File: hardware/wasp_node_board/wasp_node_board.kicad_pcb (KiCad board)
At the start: 4 copper layers, 115 parts, among them J1 Conn_01x02, J2 RJ45_Hanrun_HR911105A_Horizon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, J3 Conn_02x10_Odd_Even, J4 RJ45_Hanrun_HR911105A_Horizon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, J5 RJ45_Hanrun_HR911105A_Horizon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, J6 TC2030, J7 USB_C_Receptacle_USB2.0_16P, SW1 C&K JS102011SAQN, SW2 C&K KMR231NG LFS, U1 STM32H723ZGTx, U2 USBLC6-2SC6, U3 APS6404L-3SQRx-SN, U4 TPSM863253RDXR, U5 KSZ8794CNXCC, U6 LP5907MFX-1.2, Y1 TSX-3225 25.00M-N0YYYYG30RGB, Y2 ASE-25.000MHZ-L-K-T

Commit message: Layout half way done, starting an experiment
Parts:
- R25, Y2: moved to B.Cu
- moved J3 90.9 mm to (103.9, 54.3), turned to 0 degrees
- moved C7 86.3 mm to (126.7, 102.7), turned to 90 degrees
- moved C4 86.1 mm to (125.7, 99.0)
- moved R4 86.1 mm to (126.7, 99.0)
- moved C20 86.1 mm to (122.1, 97.7)
- moved C24 86.1 mm to (122.1, 103.2)
- moved Y1 86.1 mm to (122.1, 100.5)
- moved FB5 85.8 mm to (122.2, 93.3)
- moved C3 85.6 mm to (130.3, 102.9)
- moved C12 85.2 mm to (144.5, 55.9)
- moved C13 85.2 mm to (142.5, 55.9)
- moved C22 85.2 mm to (131.6, 53.5)
- moved C25 85.2 mm to (140.5, 55.9)
- moved C39 85.2 mm to (151.1, 55.8)
- moved C40 85.2 mm to (153.1, 55.8)
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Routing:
- net GND: track 0.00 -> 75.2 mm, vias 0 -> 34
- net Net-(U5-LED1_0): track 0.00 -> 49.0 mm, vias 0 -> 2
- net VDD12D: track 0.00 -> 41.6 mm, vias 0 -> 4
- net VDDAT: track 0.00 -> 40.8 mm, vias 0 -> 5
- net Net-(U5-LED3_1): track 0.00 -> 39.1 mm
- net /mcu/PG12: track 0.00 -> 37.2 mm, vias 0 -> 1
- net VDDIO: track 0.00 -> 36.3 mm, vias 0 -> 3
- net Net-(U5-LED2_1): track 0.00 -> 34.8 mm, vias 0 -> 2
- net /ethernet/RX1_P: track 0.00 -> 33.2 mm
- net /ethernet/RX1_N: track 0.00 -> 33.1 mm
- net ETH_RXD1: track 0.00 -> 32.1 mm, vias 0 -> 2
- net ETH_RXD0: track 0.00 -> 31.8 mm, vias 0 -> 2
- net Net-(U5-LED1_1): track 0.00 -> 31.2 mm, vias 0 -> 2
- net ETH_CRS_DV: track 0.00 -> 31.2 mm, vias 0 -> 2
- net USB_D_P: track 6.56 -> 36.6 mm
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- added copper zone on In2.Cu, net +3V3
- added copper zone on In1.Cu, net GND
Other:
- board outline added: 63.5 x 82.5 mm

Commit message: Removed some stuff and got the general placement down
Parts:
- removed A1: Arduino_UNO_R3, Arduino_UNO_R3_Headers:Arduino_UNO_R3_Headers
- removed J3: Conn_02x10_Odd_Even, Connector_PinHeader_2.54mm:PinHeader_2x10_P2.54mm_Vertical
- C22, C35, C36, C37, C38, C41, C42, C43, C44, C45, C46, C47, C48, C49, C50, C51, C52, C53, C54, C55, C56, C57, C58, C59, C60, FL1, J6, J7, R1, R2, R24, R5, U1, U2, U3: moved to B.Cu
- moved J7 60.3 mm to (158.4, 98.8), turned to -90 degrees
- moved J6 56.7 mm to (148.1, 104.1), turned to 0 degrees
- moved R2 55.4 mm to (152.6, 101.0), turned to -90 degrees
- moved C35 51.1 mm to (106.6, 85.2)
- moved U2 50.0 mm to (150.6, 99.0), turned to -90 degrees
- moved R1 49.9 mm to (152.6, 97.0), turned to 90 degrees
- moved C36 48.6 mm to (107.9, 84.6)
- moved C22 45.7 mm to (152.1, 94.3), turned to -90 degrees
- moved FL1 45.4 mm to (147.1, 99.1), turned to 180 degrees
- moved U3 43.4 mm to (110.7, 90.5), turned to 180 degrees
- moved C37 40.0 mm to (115.1, 83.7), turned to 180 degrees
- moved C43 38.5 mm to (113.3, 105.0), turned to 180 degrees
- moved Y2 38.1 mm to (110.5, 98.8)
- moved R25 38.1 mm to (112.8, 98.2)
- moved C44 38.0 mm to (113.6, 107.0), turned to 180 degrees
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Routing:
- net GND: track 75.2 -> 0.07 mm, vias 34 -> 0
- net Net-(U5-LED1_0): track 49.0 -> 0.00 mm, vias 2 -> 0
- net VDD12D: track 41.6 -> 0.00 mm, vias 4 -> 0
- net VDDAT: track 40.8 -> 0.00 mm, vias 5 -> 0
- net Net-(U5-LED3_1): track 39.1 -> 0.00 mm
- net /mcu/PG12: track 37.2 -> 0.00 mm, vias 1 -> 0
- net USB_D_P: track 36.6 -> 0.00 mm
- net USB_D_N: track 36.6 -> 0.00 mm
- net VDDIO: track 36.3 -> 0.00 mm, vias 3 -> 0
- net Net-(U5-LED2_1): track 34.8 -> 0.00 mm, vias 2 -> 0
- net ETH_RXD1: track 32.1 -> 0.00 mm, vias 2 -> 0
- net ETH_RXD0: track 31.8 -> 0.00 mm, vias 2 -> 0
- net Net-(U5-LED1_1): track 31.2 -> 0.00 mm, vias 2 -> 0
- net ETH_CRS_DV: track 31.2 -> 0.00 mm, vias 2 -> 0
- net +3V3: track 29.5 -> 0.00 mm, vias 12 -> 0
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- removed copper zone on In2.Cu, net +3V3
- removed copper zone on In1.Cu, net GND
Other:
- board size 63.5 x 82.5 mm -> 59.2 x 51.4 mm

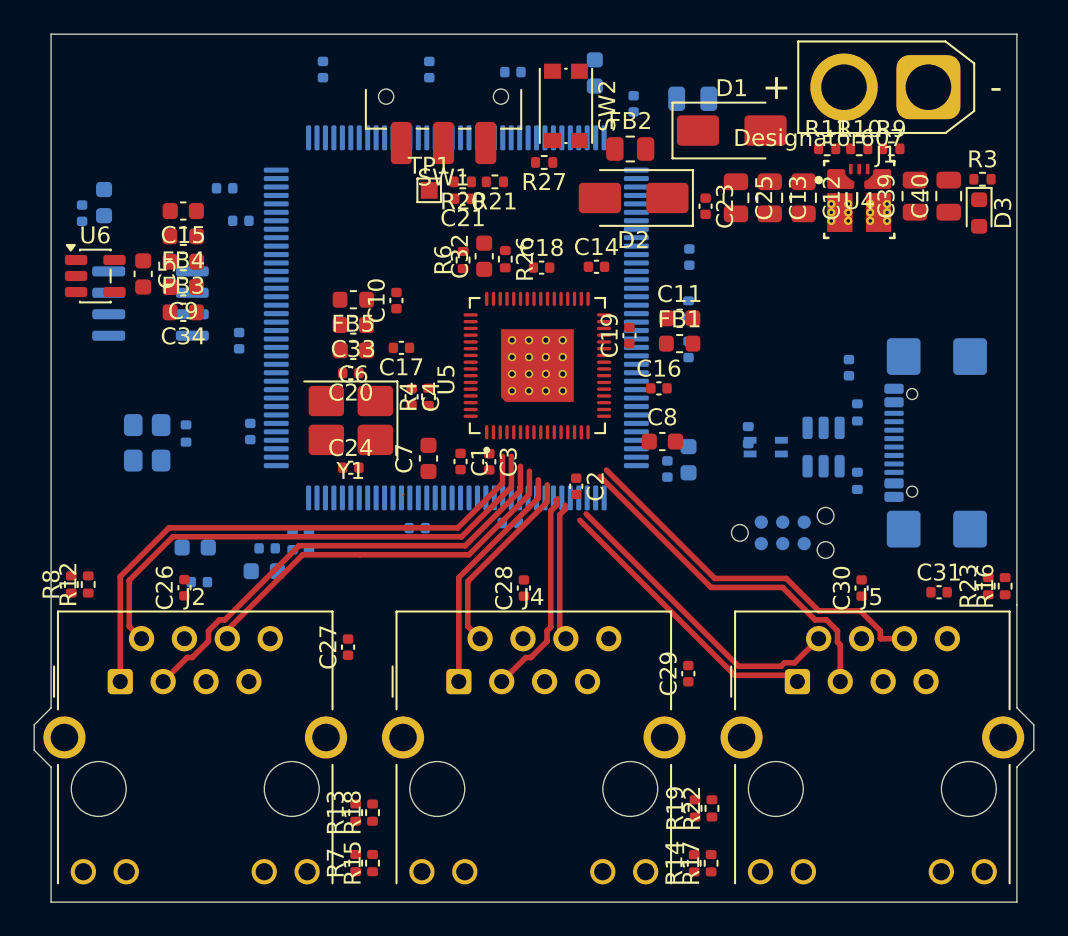
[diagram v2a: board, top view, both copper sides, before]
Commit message: Layout candidate done. Now to add back some functionality
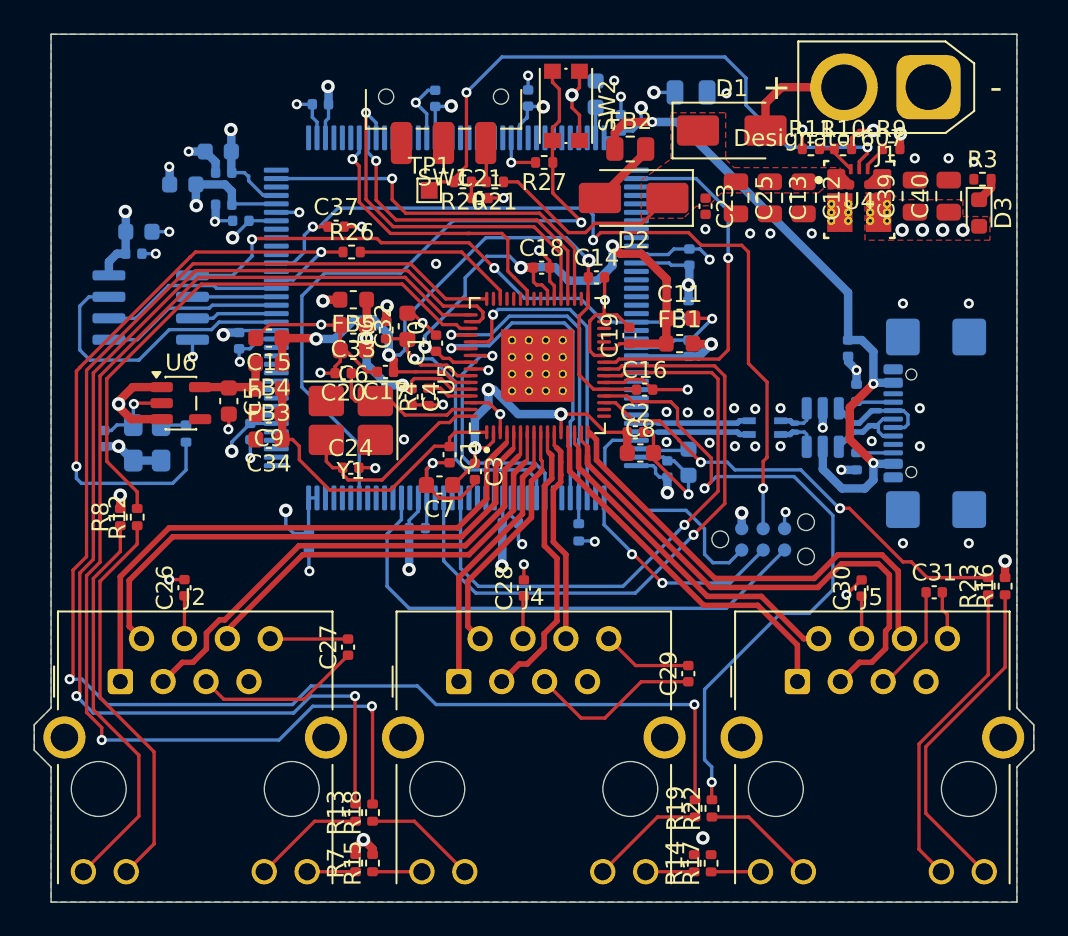
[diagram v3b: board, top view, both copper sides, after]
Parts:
- C37: moved to F.Cu
- moved C41 32.5 mm to (108.0, 98.5), turned to 90 degrees
- moved C47 29.7 mm to (133.1, 78.4), turned to 90 degrees
- moved C43 23.5 mm to (114.7, 81.5)
- moved C45 23.4 mm to (112.6, 83.5)
- moved C46 22.4 mm to (115.0, 82.8)
- moved C44 22.4 mm to (115.0, 84.7)
- moved R5 11.6 mm to (136.1, 104.1)
- moved R26 9.11 mm to (122.6, 87.5), turned to 0 degrees
- moved C15 9.08 mm to (117.7, 92.6)
- moved C34 9.08 mm to (117.7, 98.6)
- moved C5 9.08 mm to (115.3, 96.3)
- moved C9 9.08 mm to (117.7, 97.1)
- moved FB3 9.08 mm to (117.7, 95.6)
- moved FB4 9.08 mm to (117.7, 94.1)
- moved U6 9.08 mm to (112.5, 96.5)
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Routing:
- net GND: track 0.07 -> 129.6 mm, vias 0 -> 72
- net +3V3: track 0.00 -> 93.5 mm, vias 0 -> 33
- net Net-(U5-LED2_1): track 0.00 -> 90.1 mm, vias 0 -> 2
- net Net-(U5-LED1_1): track 0.00 -> 71.0 mm, vias 0 -> 2
- net Net-(U5-LED2_0): track 0.00 -> 70.4 mm, vias 0 -> 2
- net /mcu/JTAG_NRST: track 0.00 -> 50.1 mm, vias 0 -> 3
- net VDD12D: track 0.00 -> 43.0 mm, vias 0 -> 3
- net /mcu/BOOT0: track 0.00 -> 41.8 mm, vias 0 -> 1
- net Net-(U5-LED3_0): track 0.00 -> 40.4 mm, vias 0 -> 2
- net /power/USB_POWER_IN: track 0.00 -> 40.0 mm, vias 0 -> 3
- net ETH_TXD0: track 0.00 -> 38.4 mm, vias 0 -> 1
- net /mcu/PH0/REFCLK: track 0.00 -> 37.0 mm, vias 0 -> 2
- net /power/PWR_EN: track 0.00 -> 36.6 mm, vias 0 -> 2
- net ETH_TXEN: track 0.00 -> 35.8 mm, vias 0 -> 1
- net VDDIO: track 0.00 -> 34.3 mm, vias 0 -> 3
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- added copper zone on F.Cu, net +3V3
- added copper zone on In2.Cu, net +3V3
- added copper zone on F.Cu, net +5V
- added copper zone on B.Cu, net GND
- added copper zone on F.Cu, net GND
- added copper zone on In1.Cu, net GND
- added copper zone on In2.Cu, net GND

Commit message: V1 layout done
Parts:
- removed TP1: TestPoint, TestPoint:TestPoint_Pad_1.0x1.0mm
- added D4: LTST-C191KSKT, LED_SMD:LED_0603_1608Metric, F.Cu at (121.0, 77.5)
- added J8: Conn_02x05_Odd_Even, Connector_PinHeader_2.54mm:PinHeader_2x05_P2.54mm_Vertical_SMD, F.Cu at (112.5, 83.0)
- added J9: Conn_02x05_Odd_Even, Connector_PinHeader_2.54mm:PinHeader_2x05_P2.54mm_Vertical_SMD, F.Cu at (153.1, 93.7)
- added R28: 1k, Resistor_SMD:R_0402_1005Metric, F.Cu at (121.0, 81.0)
- C21, R20, R21: moved to B.Cu
- moved R20 19.5 mm to (147.9, 77.8), turned to 0 degrees
- moved C21 17.6 mm to (146.9, 78.8), turned to 180 degrees
- moved R21 15.9 mm to (146.0, 77.8), turned to 0 degrees
- moved C53 1.15 mm to (141.4, 87.8)
- moved R16 0.70 mm to (160.6, 107.3)
- moved R23 0.70 mm to (159.6, 107.3)
- moved C43 0.30 mm to (114.7, 81.2)
- moved C46 0.30 mm to (115.0, 82.5)
- moved R13 0.25 mm to (122.8, 120.5)
- moved R18 0.25 mm to (123.8, 120.5)
- moved C37 0.15 mm to (121.5, 86.0)
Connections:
- U1 pad 136: /mcu/PB6 -> /mcu/LPUART1_TX
- U1 pad 137: /mcu/PB7 -> /mcu/LPUART1_RX
- U1 pad 46: unconnected-(U1-PB0-Pad46) -> /mcu/status_led
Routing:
- net /mcu/LPUART1_RX: track 0.00 -> 48.1 mm, vias 0 -> 1
- net /mcu/LPUART1_TX: track 0.00 -> 42.2 mm, vias 0 -> 1
- net /mcu/I2C2_SDA: track 0.00 -> 37.7 mm, vias 0 -> 1
- net /mcu/PB5: track 0.00 -> 33.0 mm, vias 0 -> 1
- net /mcu/SPI2_MISO: track 0.00 -> 28.0 mm, vias 0 -> 1
- net /power/PWR_EN: track 36.6 -> 9.33 mm, vias 2 -> 1
- net /mcu/SPI2_CS: track 0.00 -> 26.0 mm, vias 0 -> 1
- net /mcu/I2C2_SCL: track 0.00 -> 25.3 mm, vias 0 -> 1
- net /mcu/SPI2_SCK: track 0.00 -> 24.0 mm, vias 0 -> 1
- net /mcu/USART3_RX: track 0.00 -> 21.7 mm, vias 0 -> 1
- net /mcu/PE9: track 0.00 -> 21.5 mm, vias 0 -> 1
- net /mcu/SPI2_MOSI: track 0.00 -> 20.8 mm, vias 0 -> 1
- net Net-(SW1-A): track 4.20 -> 23.5 mm, vias 0 -> 1
- net /mcu/USART3_TX: track 0.00 -> 15.8 mm, vias 0 -> 1
- net /mcu/PA8: track 0.00 -> 14.2 mm, vias 0 -> 1
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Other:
- board size 59.2 x 51.4 mm -> 60.4 x 51.4 mm
- board text added: "3V3"
- board text added: "BOOTSEL"
- board text added: "CSn2"
- board text added: "ETH 1"
- board text added: "ETH 2"
- board text added: "ETH 3"
- board text added: "GND"
- board text added: "MISO2"
- board text added: "MOSI2"
- board text added: "ON|OFF"
- board text added: "PA0"
- board text added: "PA8"
- board text added: "PB5"
- board text added: "PE9"
- board text added: "SCL2"
- board text added: "SCLK2"
- board text added: "SDA2"
- board text added: "STATUS"
- board text added: "U1RX"
- board text added: "U1TX"
- board text added: "U3RX"
- board text added: "U3TX"
- board text added: "WASP Board V1 © Oskar von Heideken https://github.com/oskarvh/wasp"
